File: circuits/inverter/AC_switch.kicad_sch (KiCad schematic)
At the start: 39 parts

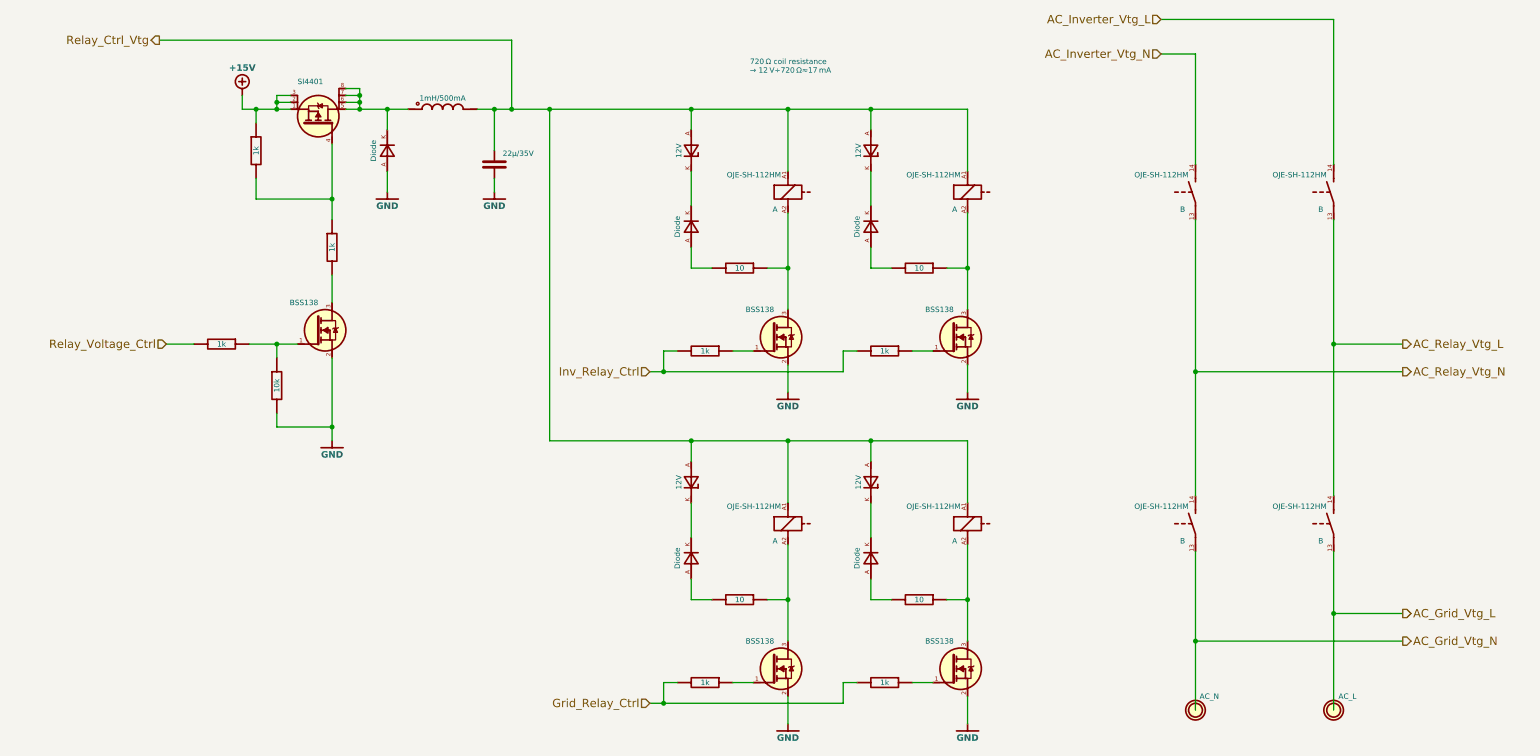
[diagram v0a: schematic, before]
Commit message: converts libraries to Kicad 6 format, updates bridge driver
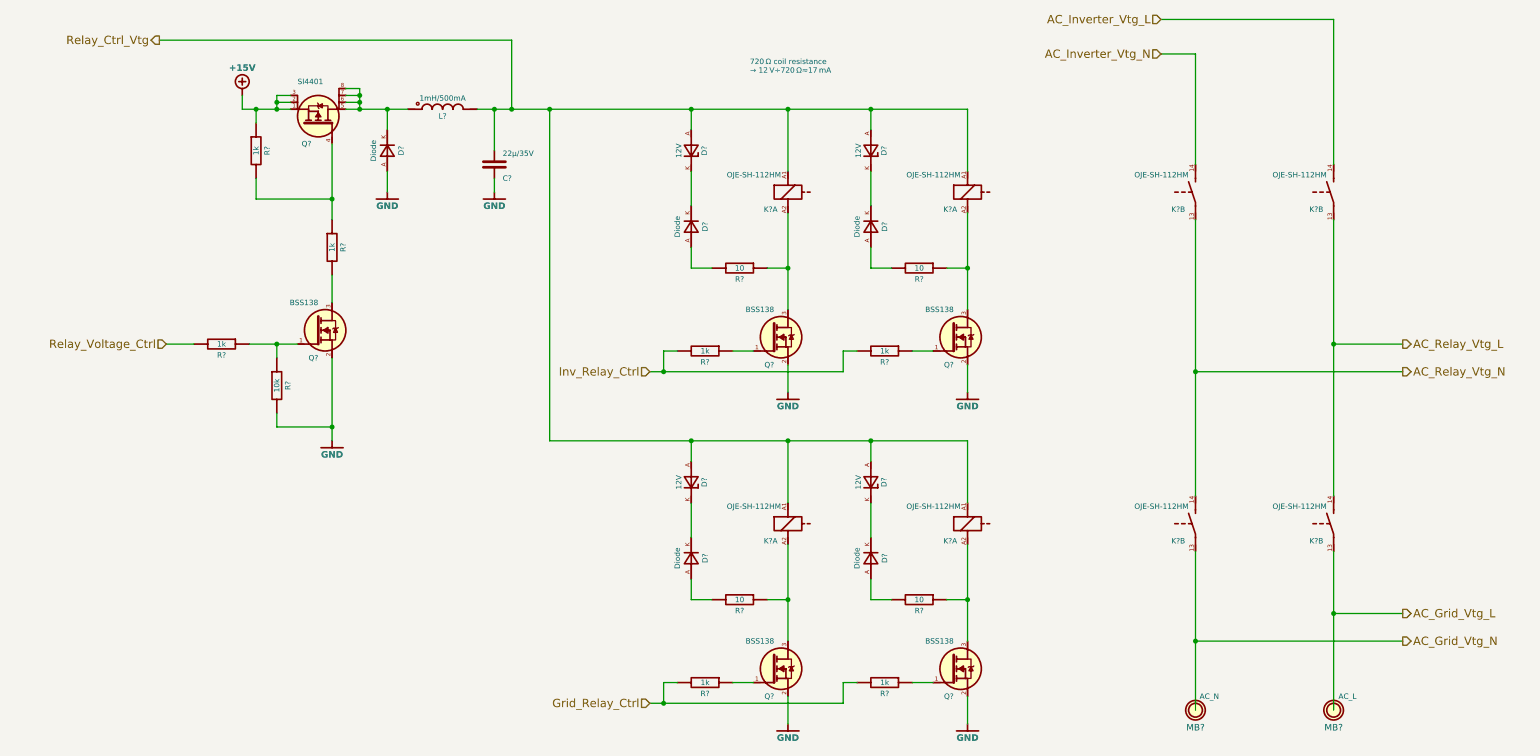
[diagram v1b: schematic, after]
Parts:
- gave numbers to parts that had none: 7
